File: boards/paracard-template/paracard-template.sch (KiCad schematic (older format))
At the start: 0 parts

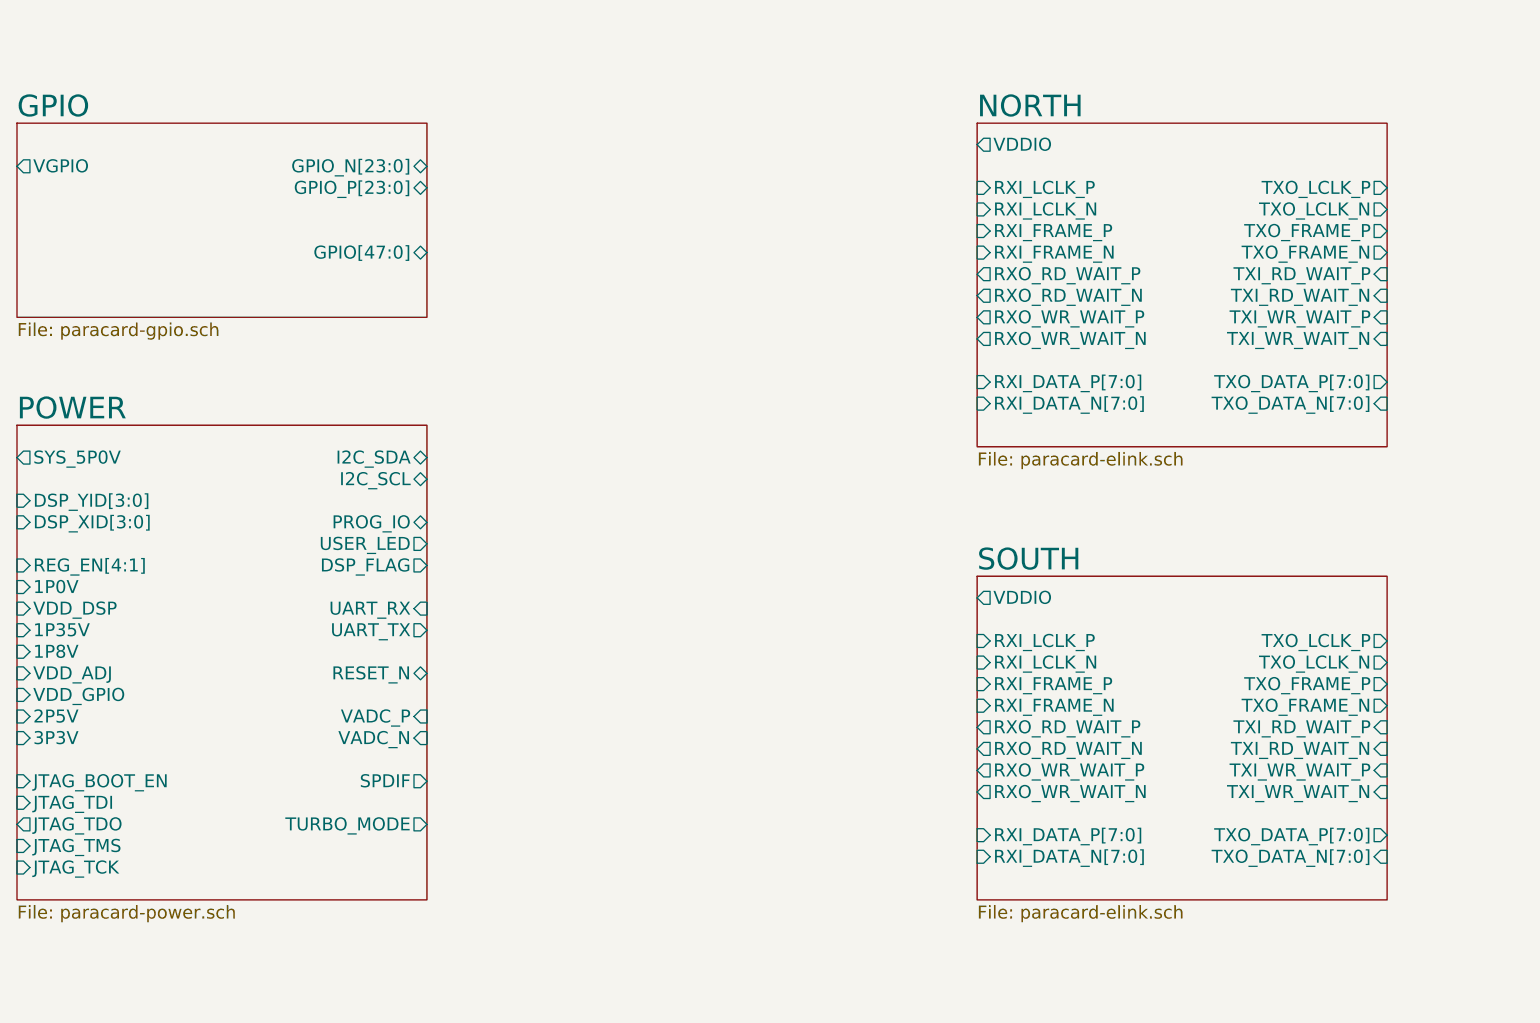
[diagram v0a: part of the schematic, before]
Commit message: Added E64 project with HDMI. Some cleanup to paracard template.
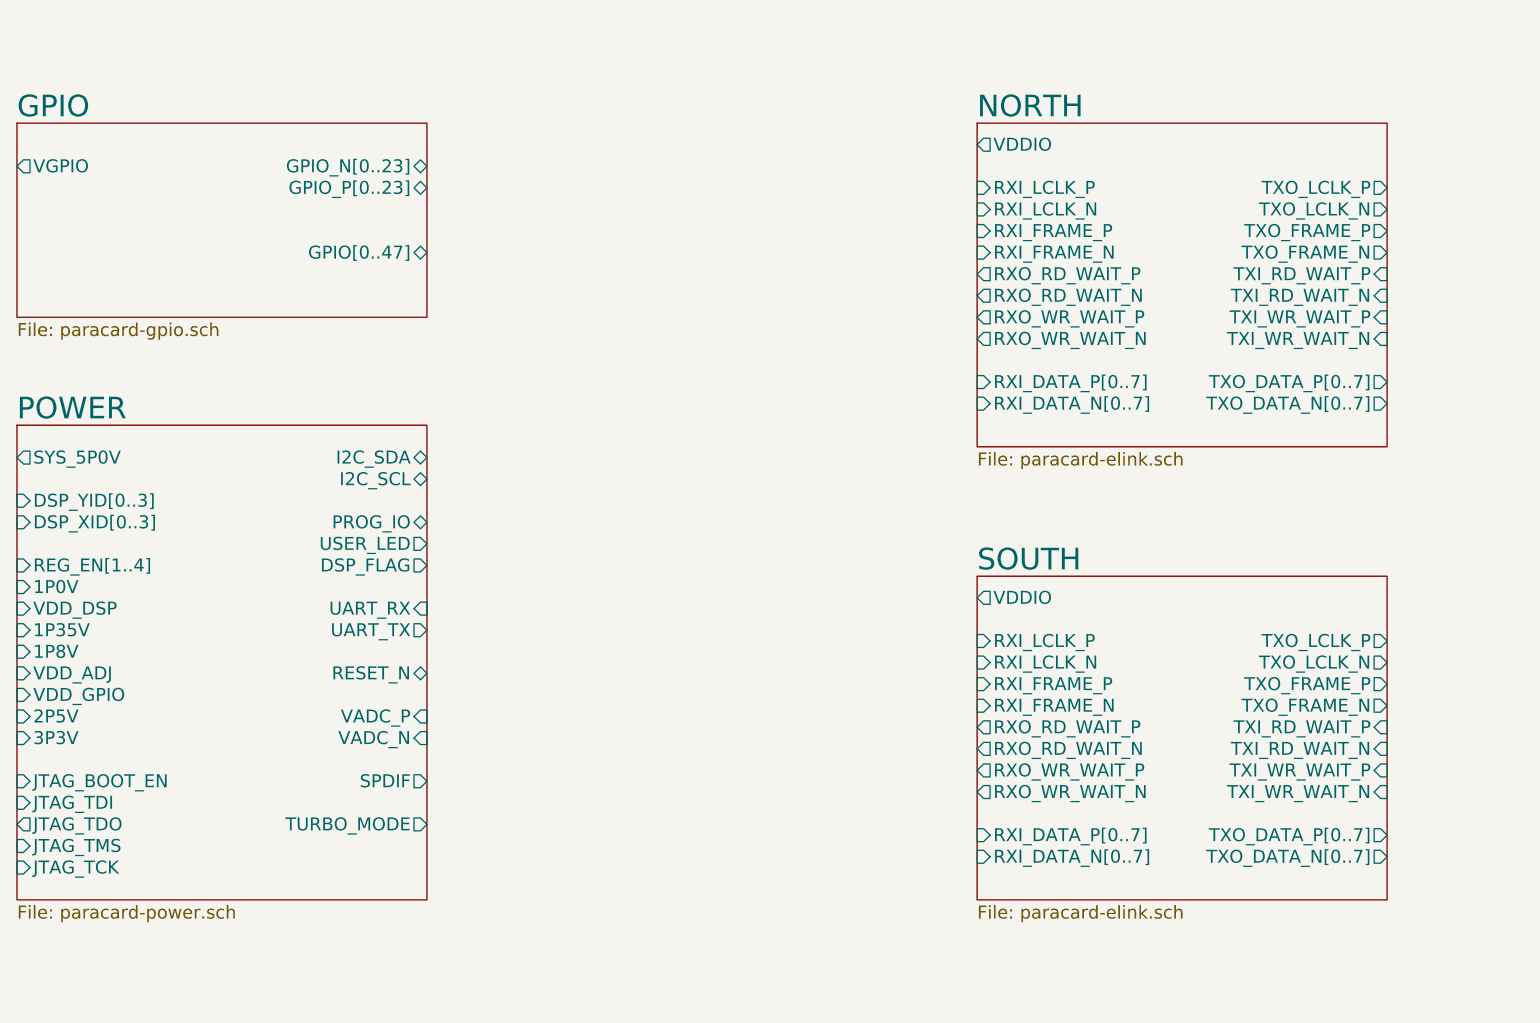
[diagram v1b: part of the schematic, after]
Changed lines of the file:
@@
 F0 "GPIO" 100
 F1 "paracard-gpio.sch" 60
-F2 "GPIO_N[23:0]" B R 5500 3250 60
-F3 "GPIO_P[23:0]" B R 5500 3350 60
-F4 "GPIO[47:0]" B R 5500 3650 60
-F5 "VGPIO" O L 3600 3250 60
+F2 "VGPIO" O L 3600 3250 60
+F3 "GPIO_N[0..23]" B R 5500 3250 60
+F4 "GPIO_P[0..23]" B R 5500 3350 60
+F5 "GPIO[0..47]" B R 5500 3650 60
 $EndSheet
 $Sheet
@@
 F17 "TXO_LCLK_N" O R 9950 3450 60
 F18 "TXO_LCLK_P" O R 9950 3350 60
-F19 "RXI_DATA_N[7:0]" I L 8050 4350 60
-F20 "RXI_DATA_P[7:0]" I L 8050 4250 60
-F21 "TXO_DATA_P[7:0]" O R 9950 4250 60
-F22 "TXO_DATA_N[7:0]" I R 9950 4350 60
+F19 "RXI_DATA_N[0..7]" I L 8050 4350 60
+F20 "RXI_DATA_P[0..7]" I L 8050 4250 60
+F21 "TXO_DATA_P[0..7]" O R 9950 4250 60
+F22 "TXO_DATA_N[0..7]" O R 9950 4350 60
 $EndSheet
 $Sheet
@@
 F2 "I2C_SDA" B R 5500 4600 60
 F3 "I2C_SCL" B R 5500 4700 60
-F4 "REG_EN[4:1]" I L 3600 5100 60
-F5 "PROG_IO" B R 5500 4900 60
-F6 "DSP_YID[3:0]" I L 3600 4800 60
-F7 "DSP_XID[3:0]" I L 3600 4900 60
-F8 "UART_RX" I R 5500 5300 60
-F9 "UART_TX" O R 5500 5400 60
-F10 "USER_LED" O R 5500 5000 60
-F11 "RESET_N" B R 5500 5600 60
-F12 "VADC_P" I R 5500 5800 60
-F13 "JTAG_TDI" I L 3600 6200 60
-F14 "JTAG_TDO" O L 3600 6300 60
-F15 "DSP_FLAG" O R 5500 5100 60
-F16 "TURBO_MODE" O R 5500 6300 60
-F17 "SPDIF" O R 5500 6100 60
-F18 "JTAG_BOOT_EN" I L 3600 6100 60
-F19 "VADC_N" I R 5500 5900 60
-F20 "JTAG_TMS" I L 3600 6400 60
-F21 "JTAG_TCK" I L 3600 6500 60
-F22 "1P0V" I L 3600 5200 60
-F23 "VDD_DSP" I L 3600 5300 60
-F24 "1P35V" I L 3600 5400 60
-F25 "1P8V" I L 3600 5500 60
-F26 "VDD_ADJ" I L 3600 5600 60
-F27 "VDD_GPIO" I L 3600 5700 60
-F28 "2P5V" I L 3600 5800 60
-F29 "3P3V" I L 3600 5900 60
-F30 "SYS_5P0V" O L 3600 4600 60
+F4 "PROG_IO" B R 5500 4900 60
+F5 "UART_RX" I R 5500 5300 60
+F6 "UART_TX" O R 5500 5400 60
+F7 "USER_LED" O R 5500 5000 60
+F8 "RESET_N" B R 5500 5600 60
+F9 "VADC_P" I R 5500 5800 60
+F10 "JTAG_TDI" I L 3600 6200 60
+F11 "JTAG_TDO" O L 3600 6300 60
+F12 "DSP_FLAG" O R 5500 5100 60
+F13 "TURBO_MODE" O R 5500 6300 60
+F14 "SPDIF" O R 5500 6100 60
+F15 "JTAG_BOOT_EN" I L 3600 6100 60
+F16 "VADC_N" I R 5500 5900 60
+F17 "JTAG_TMS" I L 3600 6400 60
+F18 "JTAG_TCK" I L 3600 6500 60
+F19 "1P0V" I L 3600 5200 60
+F20 "VDD_DSP" I L 3600 5300 60
+F21 "1P35V" I L 3600 5400 60
+F22 "1P8V" I L 3600 5500 60
+F23 "VDD_ADJ" I L 3600 5600 60
+F24 "VDD_GPIO" I L 3600 5700 60
+F25 "2P5V" I L 3600 5800 60
+F26 "3P3V" I L 3600 5900 60
+F27 "SYS_5P0V" O L 3600 4600 60
+F28 "REG_EN[1..4]" I L 3600 5100 60
+F29 "DSP_YID[0..3]" I L 3600 4800 60
+F30 "DSP_XID[0..3]" I L 3600 4900 60
 $EndSheet
 $Sheet
+S 3600 7450 1950 700
+U 5387F901
+F0 "MountingHoles" 100
+F1 "paracard-mtg.sch" 60
+F2 "SYS_5P0V" O L 3600 7600 60
+$EndSheet
+Text Notes 11950 3500 0    60   ~ 0
+POWER PAD
+Wire Notes Line
+	12050 3500 12150 3600
+Wire Notes Line
+	12150 3600 12150 3550
+Wire Notes Line
+	12150 3600 12100 3600
+$Sheet
 S 8050 5150 1900 1500
-U 5387844C
+U 538E9511
 F0 "SOUTH" 100
 F1 "paracard-elink.sch" 60
@@
 F17 "TXO_LCLK_N" O R 9950 5550 60
 F18 "TXO_LCLK_P" O R 9950 5450 60
-F19 "RXI_DATA_N[7:0]" I L 8050 6450 60
-F20 "RXI_DATA_P[7:0]" I L 8050 6350 60
-F21 "TXO_DATA_P[7:0]" O R 9950 6350 60
-F22 "TXO_DATA_N[7:0]" I R 9950 6450 60
+F19 "RXI_DATA_N[0..7]" I L 8050 6450 60
+F20 "RXI_DATA_P[0..7]" I L 8050 6350 60
+F21 "TXO_DATA_P[0..7]" O R 9950 6350 60
+F22 "TXO_DATA_N[0..7]" O R 9950 6450 60
 $EndSheet
-$Sheet
-S 3600 7450 1950 700
-U 5387F901
-F0 "MountingHoles" 100
-F1 "paracard-mtg.sch" 60
-F2 "SYS_5P0V" O L 3600 7600 60
-$EndSheet
-Text Notes 11950 3500 0    60   ~ 0
-POWER PAD
-Wire Notes Line
-	12050 3500 12150 3600
-Wire Notes Line
-	12150 3600 12150 3550
-Wire Notes Line
-	12150 3600 12100 3600
 $EndSCHEMATC

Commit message: Ready for full review.
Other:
- note added: ""Paracard" Daughtercard template for\nAdapteva Parallella-I.\nThis schematic and associated PCB\ndesign may be used as a starting point\nfor Parallella-I daughtercard design.\n\nThis work is licensed under Creative Commons Attribution-Share Alike 3.0\nUnprotected License. To view a copy of this license, visit \nhttp://creativecommons.org/licenses/by-sa/3.0/ or send a letter to \nCreative Commons,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"
- note removed: ""Paracard" Daughtercard template for\nAdapteva Parallella-I.\nThis schematic and associated PCB\ndesign may be used as a starting point\nfor Parallella-I daughtercard design.\n\n<Add license here>\n"
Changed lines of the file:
@@
 Wire Notes Line
 	15200 2200 15200 1550
-Text Notes 12800 7200 0    100  ~ 0
-"Paracard" Daughtercard template for\nAdapteva Parallella-I.\nThis schematic and associated PCB\ndesign may be used as a starting point\nfor Parallella-I daughtercard design.\n\n<Add license here>\n
+Text Notes 11000 8750 0    80   ~ 0
+"Paracard" Daughtercard template for\nAdapteva Parallella-I.\nThis schematic and associated PCB\ndesign may be used as a starting point\nfor Parallella-I daughtercard design.\n\nThis work is licensed under Creative Commons Attribution-Share Alike 3.0\nUnprotected License.  To view a copy of this license, visit \nhttp://creativecommons.org/licenses/by-sa/3.0/ or send a letter to \nCreative Commons, 171 Second Street, Suite 300, San Francisco, California,\n94105, USA.\n\nThis schematic is *NOT SUPPORTED* and DOES NOT constitute a reference design.\nOnly *community* support is allowed via resources at forums.parallella.org.\nTHERE IS NO WARRANTY FOR THIS DESIGN, TO THE EXTENT PERMITTED\nBY APPLICABLE LAW. EXCEPT WHEN OTHERWISE STATED IN WRITING THE\nCOPYRIGHT HOLDERS AND/OR OTHER PARTIES PROVIDE THE DESIGN *AS IS*\nWITHOUT WARRANTY OF ANY KIND, EITHER EXPRESSED OR IMPLIED, INCLUDING,\nBUT NOT LIMITED TO, THE IMPLIED WARRANTIES OF MERCHANTABILITY AND\nFITNESS FOR A PARTICULAR PURPOSE. THE ENTIRE RISK AS TO THE QUALITY\nOF PERFORMANCE OF THE DESIGN IS WITH YOU. SHOULD THE DESIGN PROVE\nDEFECTIVE, YOU ASSUME THE COST OF ALL NECESSARY SERVICING,\nREPAIR OR CORRECTION.
 $Sheet
 S 3600 3050 1900 900
@@
 F29 "DSP_YID[0..3]" I L 3600 4800 60
 F30 "DSP_XID[0..3]" I L 3600 4900 60
+F31 "SPARE" B R 5500 6400 60
 $EndSheet
 $Sheet
